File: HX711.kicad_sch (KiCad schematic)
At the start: 18 parts, among them J8 Conn_01x04_Pin, J9 Conn_01x04_Pin, Q1 MMBT3906, U5 HX711

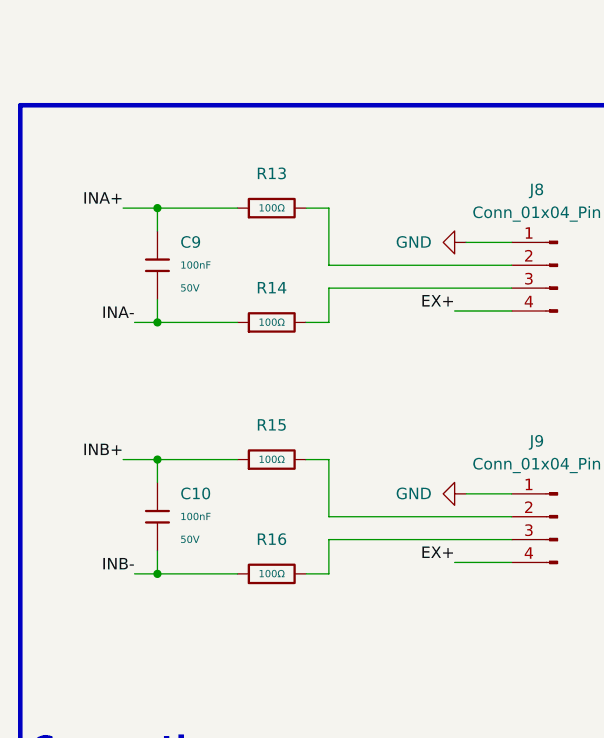
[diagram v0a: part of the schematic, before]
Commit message: finished routing and exported gerber
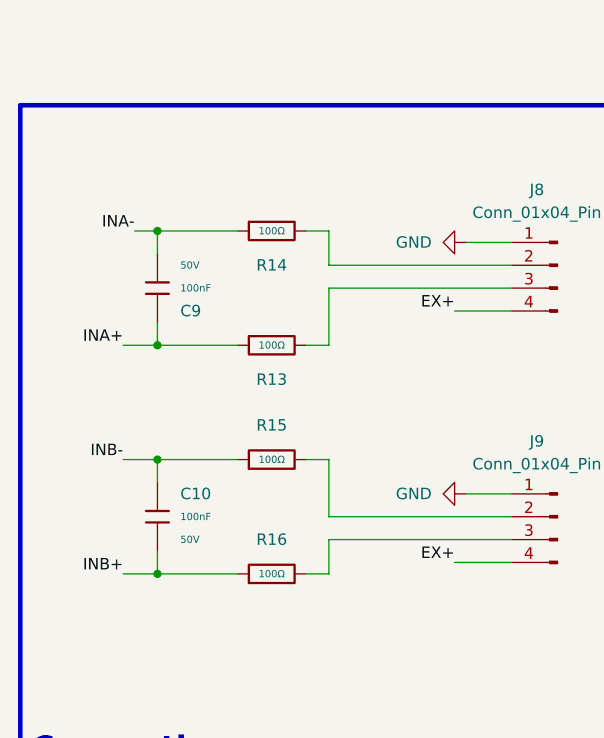
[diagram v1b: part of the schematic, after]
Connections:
- net INB+: now also C10.2, R16.1; no longer C10.1, R15.1
- net INB-: now also C10.1, R15.1; no longer C10.2, R16.1
- net at R14.2: now also J8.2 (Pin_2); no longer J8.3 (Pin_3)
- net at R13.2: now also J8.3 (Pin_3); no longer J8.2 (Pin_2)
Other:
- moved on the sheet: C9, R13, R14
